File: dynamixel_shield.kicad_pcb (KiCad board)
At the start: 2 copper layers, 68.6 x 53.3 mm, 31 parts, among them P1 BARREL_JACK, P2 CONN_01X02, P3 CONN_01X03, P4 CONN_01X03, P5 CONN_01X03, P6 CONN_01X03, P7 CONN_01X03, P8 CONN_01X03, P9 CONN_01X03, Q1 MOSFET_N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

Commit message: add a few vias between ground planes
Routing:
- net GND: track 5.98 -> 45.5 mm, vias 2 -> 7
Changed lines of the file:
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@@
     (thickness 1.6)
     (drawings 19)
-    (tracks 221)
+    (tracks 241)
     (zones 0)
     (modules 31)
@@
   (segment (start 110.744 99.06) (end 105.664 104.14) (width 1.5) (layer F.Cu) (net 10))
   (segment (start 105.664 104.14) (end 105.664 104.648) (width 1.5) (layer F.Cu) (net 10))
+  (segment (start 120.904 88.432) (end 121.1345 88.432) (width 0.25) (layer B.Cu) (net 11))
+  (segment (start 121.1345 88.432) (end 121.158 88.4555) (width 0.25) (layer B.Cu) (net 11))
+  (segment (start 121.158 88.4555) (end 124.333 88.4555) (width 0.25) (layer B.Cu) (net 11))
+  (segment (start 124.333 88.4555) (end 124.6505 88.773) (width 0.25) (layer B.Cu) (net 11))
+  (segment (start 124.6505 88.773) (end 124.6505 93.218) (width 0.25) (layer B.Cu) (net 11))
+  (segment (start 124.6505 93.218) (end 118.999 98.8695) (width 0.25) (layer B.Cu) (net 11))
+  (via (at 118.999 98.8695) (size 0.6) (drill 0.4) (layers F.Cu B.Cu) (net 11))
+  (segment (start 77.64 103.886) (end 77.64 102.954) (width 0.25) (layer F.Cu) (net 11))
+  (via (at 82.2325 100.584) (size 0.6) (drill 0.4) (layers F.Cu B.Cu) (net 11))
+  (segment (start 80.01 100.584) (end 82.2325 100.584) (width 0.25) (layer F.Cu) (net 11))
+  (segment (start 77.64 102.954) (end 80.01 100.584) (width 0.25) (layer F.Cu) (net 11))
+  (segment (start 120.904 77.256) (end 120.904 74.8665) (width 0.25) (layer F.Cu) (net 11))
+  (via (at 118.11 72.0725) (size 0.6) (drill 0.4) (layers F.Cu B.Cu) (net 11))
+  (segment (start 120.904 74.8665) (end 118.11 72.0725) (width 0.25) (layer F.Cu) (net 11))
+  (segment (start 106.212 85.852) (end 106.212 89.241) (width 0.25) (layer B.Cu) (net 11))
+  (via (at 104.521 90.932) (size 0.6) (drill 0.4) (layers F.Cu B.Cu) (net 11))
+  (segment (start 106.212 89.241) (end 104.521 90.932) (width 0.25) (layer B.Cu) (net 11))
+  (segment (start 84.328 82.55) (end 86.2965 82.55) (width 0.25) (layer F.Cu) (net 11))
+  (via (at 88.138 80.7085) (size 0.6) (drill 0.4) (layers F.Cu B.Cu) (net 11))
+  (segment (start 86.2965 82.55) (end 88.138 80.7085) (width 0.25) (layer F.Cu) (net 11))
   (segment (start 80.307 70.104) (end 77.597 70.104) (width 0.25) (layer F.Cu) (net 11))
   (via (at 77.597 70.104) (size 0.6) (drill 0.4) (layers F.Cu B.Cu) (net 11))

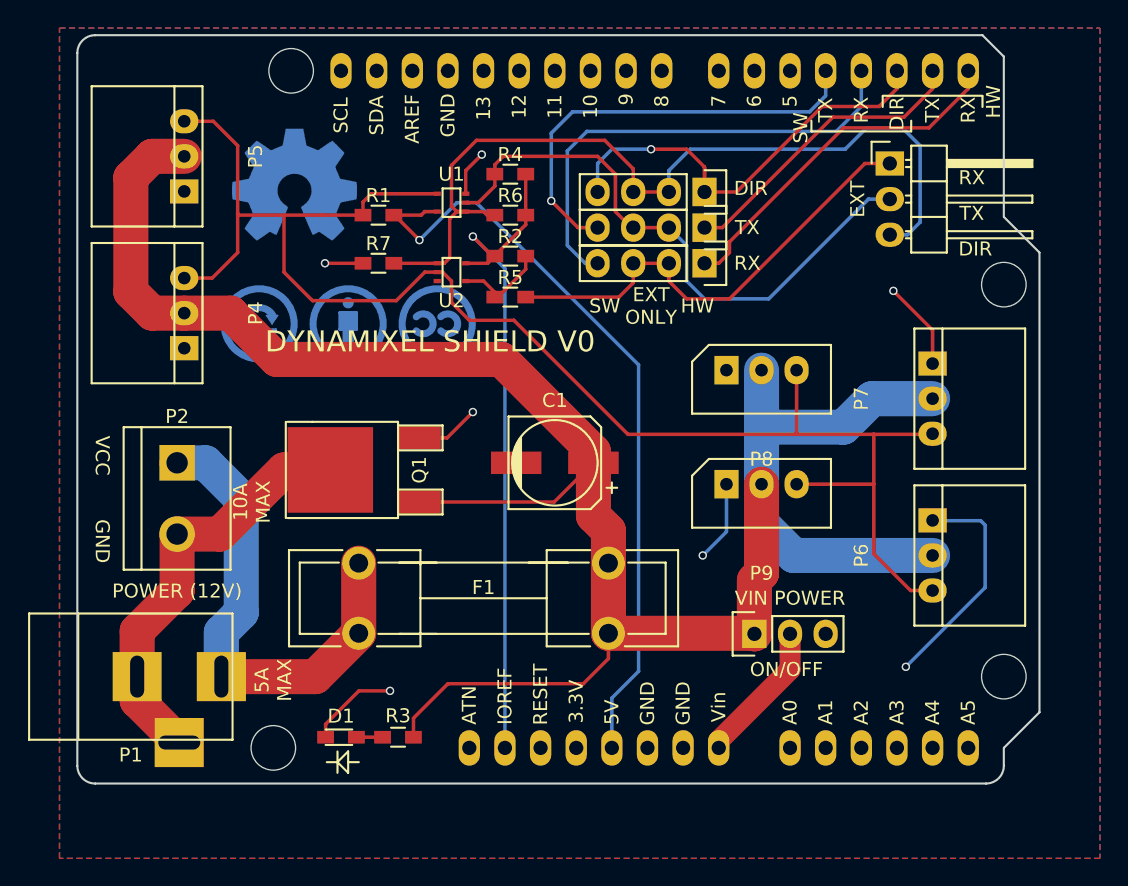
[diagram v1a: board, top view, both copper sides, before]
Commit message: tweak some components placement
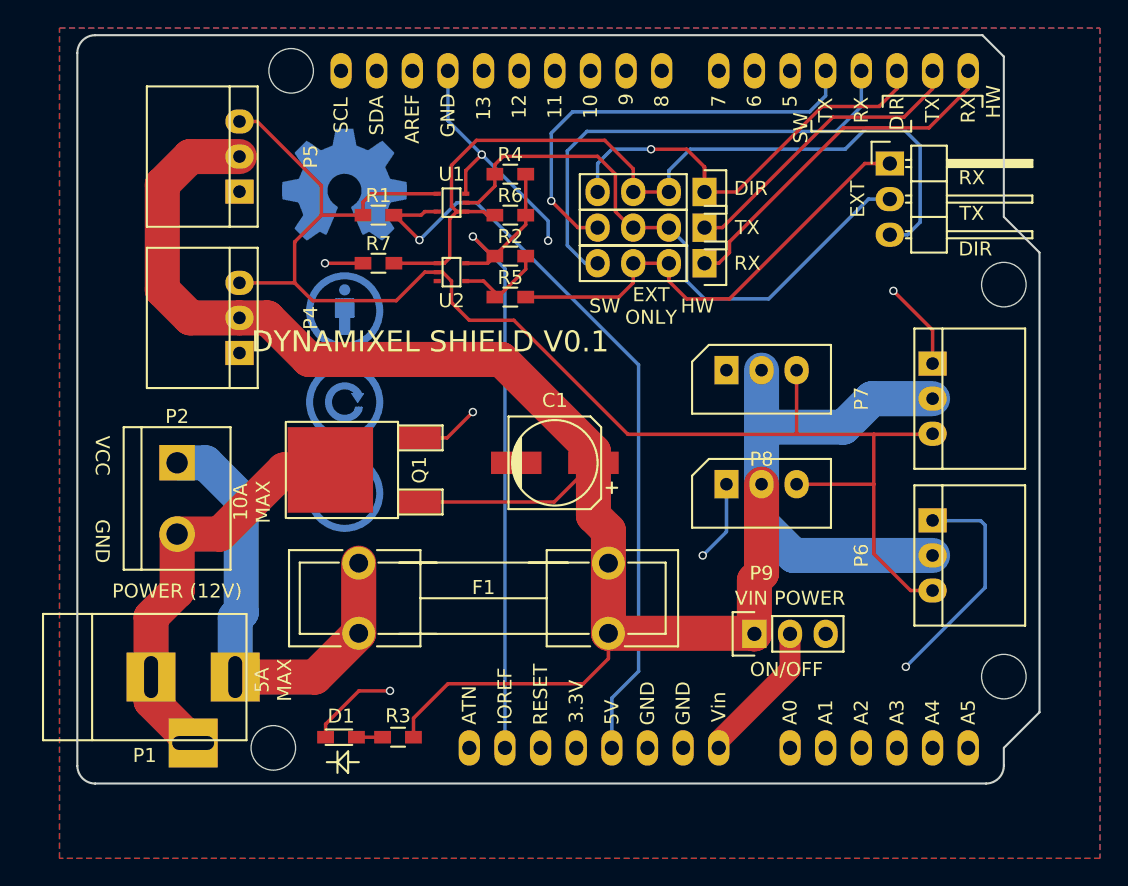
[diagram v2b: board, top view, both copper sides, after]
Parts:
- moved REF** 13.8 mm to (79.0, 86.5)
- moved REF** 8.27 mm to (79.0, 80.0)
- moved P4 3.95 mm to (71.5, 74.0)
- moved P5 3.94 mm to (71.5, 62.5)
- moved REF*** 3.56 mm to (79.0, 64.5)
- moved P1 0.99 mm to (65.0, 99.6)
- moved REF** 0.95 mm to (79.0, 73.5)
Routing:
- net GND: track 45.5 -> 60.6 mm, vias 7 -> 8
- net /DATA: track 113.8 -> 105.2 mm
- net Net-(F1-Pad1): track 35.0 -> 33.7 mm
- net +12V: track 154.4 -> 153.5 mm
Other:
- board text added: "DYNAMIXEL SHIELD V0.1"
- board text removed: "DYNAMIXEL SHIELD V0"

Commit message: increase capacitors, add a few vias
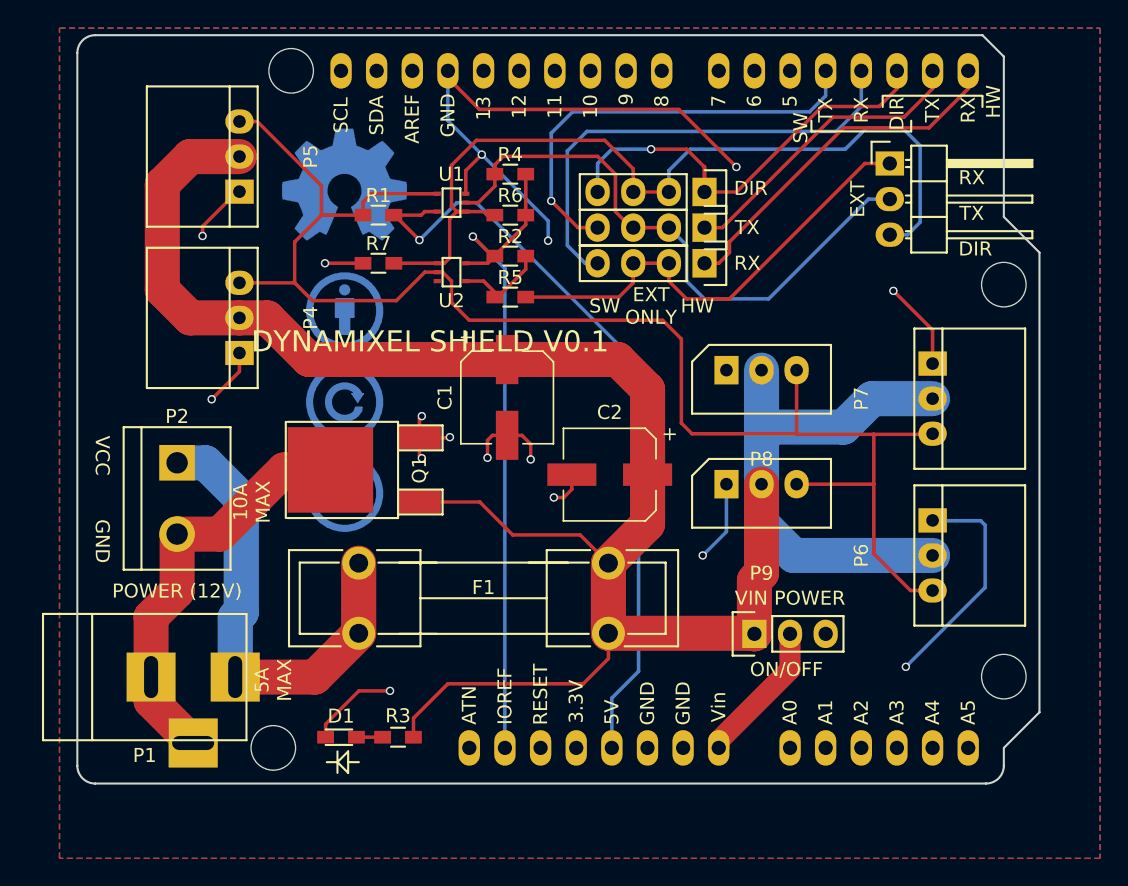
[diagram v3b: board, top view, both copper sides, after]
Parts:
- added C2: 220uF, Capacitors_SMD:CP_Elec_6.3x7.7, F.Cu at (97.9, 85.2)
- C1: value 47uF -> 220uF; footprint Capacitors_SMD:c_elec_6.3x5.8 -> Capacitors_SMD:CP_Elec_6.3x7.7
- R5: value 500 -> 200
- moved C1 5.77 mm to (90.6, 79.7), turned to 270 degrees
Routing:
- net GND: track 60.6 -> 101.9 mm, vias 8 -> 16
- net +12V: track 153.5 -> 167.8 mm
- net /DATA: track 105.2 -> 108.7 mm
